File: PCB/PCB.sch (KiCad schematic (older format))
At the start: 46 parts, among them J1 Conn_01x04_Female, J10 Conn_01x08_Female, J11 Conn_01x01_Female, J12 Conn_01x04_Female, J13 Conn_01x02_Female, J2 Conn_01x28_Female, J3 Conn_01x02_Female, J4 Conn_01x02_Female, J5 Conn_01x02_Female, J6 Conn_01x02_Female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

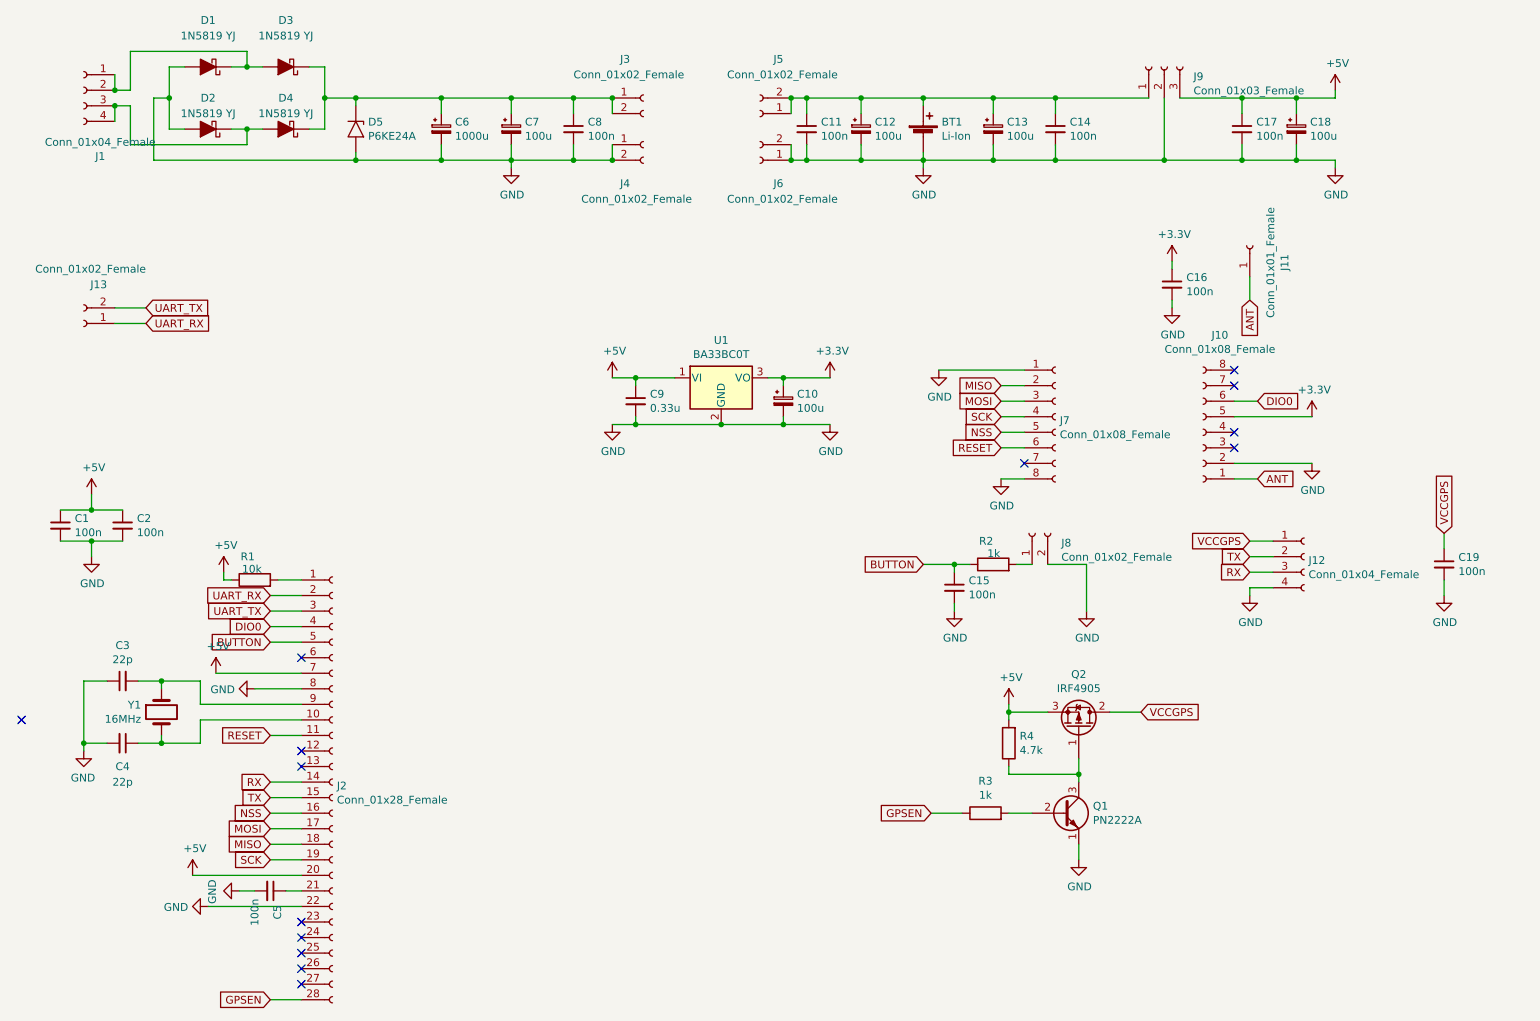
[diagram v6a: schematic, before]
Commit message: Added batter measuring resistor
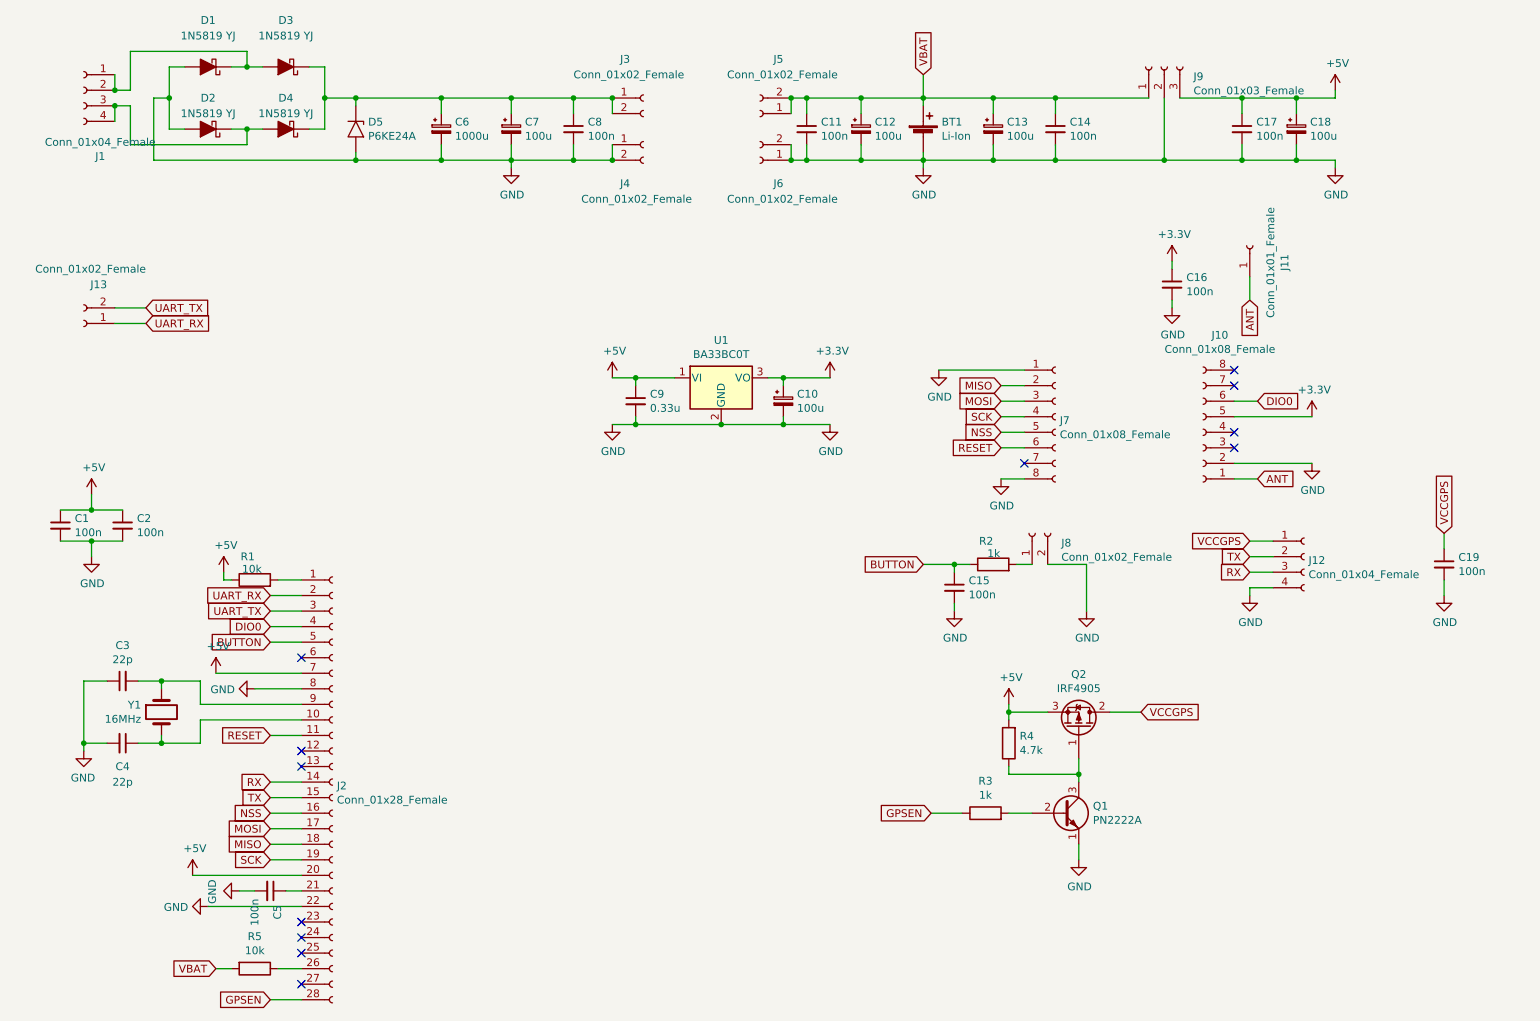
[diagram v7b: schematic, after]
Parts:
- added R5: 10k, Resistor_THT:R_Axial_DIN0207_L6.3mm_D2.5mm_P10.16mm_Horizontal, symbol Device:R
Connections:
- net VBAT: now reaches BT1.1 (+), C11.1, C12.1, C13.1, C14.1, J5.1 (Pin_1), J5.2 (Pin_2), J9.1 (Pin_1)
- net VBAT: now also R5.2
- net at J2.26 (Pin_26): now also R5.1
- no-connect marks 14 -> 12
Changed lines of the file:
@@
 	2750 6350 2850 6350
 NoConn ~ 2850 6750
-NoConn ~ 2850 6850
 NoConn ~ 2850 6950
 $Comp
@@
 Connection ~ 1650 1300
 NoConn ~ 8850 3100
-NoConn ~ 1050 5250
 $Comp
 L Connector:Conn_01x02_Female J13
@@
 Wire Wire Line
 	1650 2600 1850 2600
+$Comp
+L Device:R R5
+U 1 1 5E3486A5
+P 2550 6850
+F 0 "R5" V 2343 6850 50  0000 C CNN
+F 1 "10k" V 2434 6850 50  0000 C CNN
+F 2 "Resistor_THT:R_Axial_DIN0207_L6.3mm_D2.5mm_P10.16mm_Horizontal" V 2480 6850 50  0001 C CNN
+F 3 "~" H 2550 6850 50  0001 C CNN
+	1    2550 6850
+	0    1    1    0
+$EndComp
+Text GLabel 6850 1100 1    50   Input ~ 0
+VBAT
+Wire Wire Line
+	6850 1100 6850 1250
+Wire Wire Line
+	2700 6850 2850 6850
+Wire Wire Line
+	2400 6850 2300 6850
+Text GLabel 2300 6850 0    50   Input ~ 0
+VBAT
 $EndSCHEMATC
